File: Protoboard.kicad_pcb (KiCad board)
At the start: 2 copper layers, 103 x 140 mm, 92 parts, among them P1 CONN_01X08, P2 CONN_01X04, P3 CONN_01X05, P5 CONN_02X05, U1 LoLin_V3

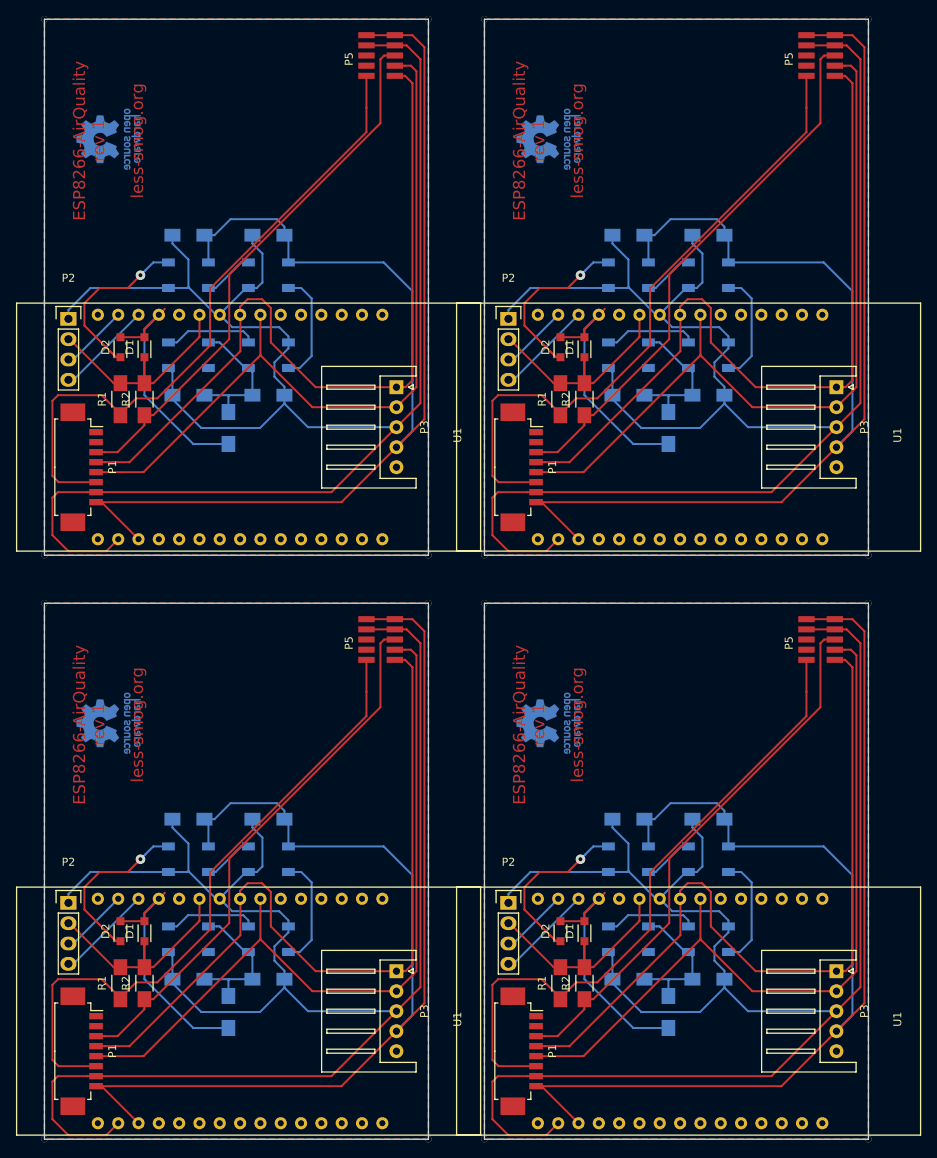
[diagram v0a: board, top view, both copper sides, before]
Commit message: Tigten boards together to fix on a 10x16 cm board.
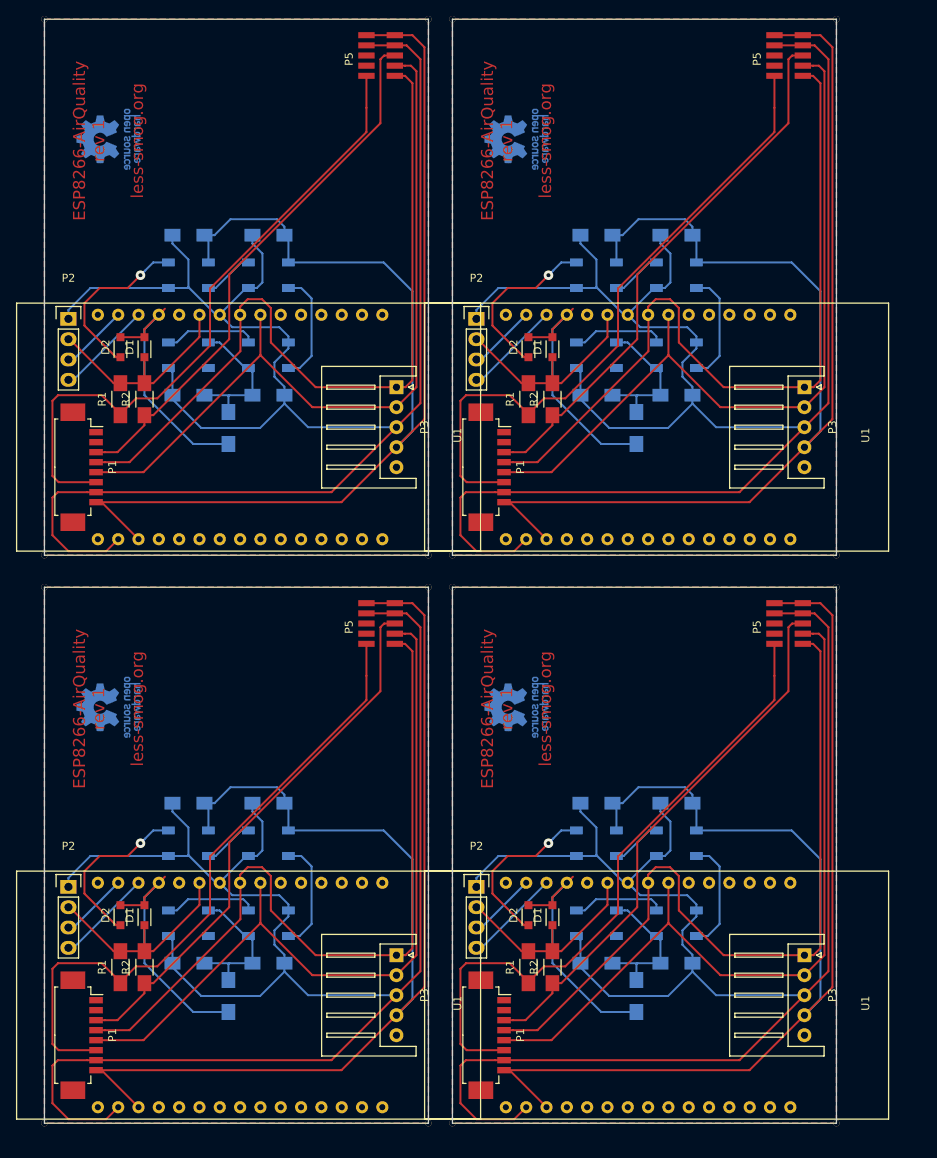
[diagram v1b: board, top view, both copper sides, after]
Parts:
- removed the ? at (74.1, 19.9)
- removed the ? at (74.1, 86.9)
- removed the ? at (74.1, 159.9)
- removed the ? at (19.1, 159.9)
- removed the ? at (67.1, 159.9)
- removed the ? at (67.1, 92.9)
- removed the ? at (19.1, 92.9)
- removed the ? at (74.1, 92.9)
- removed the ? at (122.1, 19.9)
- removed the ? at (122.1, 92.9)
- removed the ? at (122.1, 86.9)
- removed the ? at (122.1, 159.9)
- removed the C1 at (92.1, 46.9)
- removed the C1 at (92.1, 119.9)
- removed the C1 at (37.1, 119.9)
- removed the C2 at (102.1, 46.9)
- removed the C2 at (102.1, 119.9)
- removed the C2 at (47.1, 119.9)
- removed the C3 at (102.1, 66.9)
- removed the C3 at (102.1, 139.9)
- removed the C3 at (47.1, 139.9)
- removed the C4 at (92.1, 66.9)
- removed the C4 at (92.1, 139.9)
- removed the C4 at (37.1, 139.9)
- removed the D1 at (86.6, 60.9)
- removed the D1 at (86.6, 133.9)
- removed the D1 at (31.6, 133.9)
- removed the D2 at (83.6, 60.9)
- removed the D2 at (83.6, 133.9)
- removed the D2 at (28.6, 133.9)
- removed the LED1 at (92.1, 51.9)
- removed the LED1 at (92.1, 124.9)
- removed the LED1 at (37.1, 124.9)
- removed the LED2 at (102.1, 51.9)
- removed the LED2 at (102.1, 124.9)
- removed the LED2 at (47.1, 124.9)
- removed the LED3 at (102.1, 61.9)
- removed the LED3 at (102.1, 134.9)
- removed the LED3 at (47.1, 134.9)
- removed the LED4 at (92.1, 61.9)
- removed the LED4 at (92.1, 134.9)
- removed the LED4 at (37.1, 134.9)
- removed the P1 at (79.1, 75.9)
- removed the P1 at (79.1, 148.9)
- removed the P1 at (24.1, 148.9)
- removed the P2 at (77.1, 57.4)
- removed the P2 at (77.1, 130.4)
- removed the P2 at (22.1, 130.4)
- removed the P3 at (118.1, 65.9)
- removed the P3 at (118.1, 138.9)
- removed the P3 at (63.1, 138.9)
- removed the P5 at (114.3, 21.9)
- removed the P5 at (114.3, 94.9)
- removed the P5 at (59.3, 94.9)
- removed the R1 at (83.6, 67.4)
- removed the R1 at (83.6, 140.4)
- removed the R1 at (28.6, 140.4)
- removed the R2 at (86.6, 67.4)
- removed the R2 at (86.6, 140.4)
- removed the R2 at (31.6, 140.4)
- removed the R3 at (97.1, 71.0)
- removed the R3 at (97.1, 144.0)
- removed the R3 at (42.1, 144.0)
- removed the REF*** at (82.1, 34.9)
- removed the REF*** at (82.1, 107.9)
- removed the REF*** at (27.1, 107.9)
- removed the U1 at (70.6, 86.7)
- removed the U1 at (70.6, 159.7)
- removed the U1 at (15.6, 159.7)
- added ?: , Wire_Pads:SolderWirePad_single_0-8mmDrill, F.Cu at (118.1, 90.9)
- added ?: , Wire_Pads:SolderWirePad_single_0-8mmDrill, F.Cu at (70.1, 157.9)
- added ?: , Wire_Pads:SolderWirePad_single_0-8mmDrill, F.Cu at (19.1, 157.9)
- added ?: , Wire_Pads:SolderWirePad_single_0-8mmDrill, F.Cu at (70.1, 86.9)
- added ?: , Wire_Pads:SolderWirePad_single_0-8mmDrill, F.Cu at (67.1, 90.9)
- added ?: , Wire_Pads:SolderWirePad_single_0-8mmDrill, F.Cu at (118.1, 19.9)
- added ?: , Wire_Pads:SolderWirePad_single_0-8mmDrill, F.Cu at (70.1, 90.9)
- added ?: , Wire_Pads:SolderWirePad_single_0-8mmDrill, F.Cu at (19.1, 90.9)
- added ?: , Wire_Pads:SolderWirePad_single_0-8mmDrill, F.Cu at (70.1, 19.9)
- added ?: , Wire_Pads:SolderWirePad_single_0-8mmDrill, F.Cu at (118.1, 157.9)
- added ?: , Wire_Pads:SolderWirePad_single_0-8mmDrill, F.Cu at (67.1, 157.9)
- added ?: , Wire_Pads:SolderWirePad_single_0-8mmDrill, F.Cu at (118.1, 86.9)
- added C1: 100nF, Capacitors_SMD:C_1206_HandSoldering, B.Cu at (88.1, 117.9)
- added C1: 100nF, Capacitors_SMD:C_1206_HandSoldering, B.Cu at (37.1, 117.9)
- added C1: 100nF, Capacitors_SMD:C_1206_HandSoldering, B.Cu at (88.1, 46.9)
- added C2: 100nF, Capacitors_SMD:C_1206_HandSoldering, B.Cu at (98.1, 117.9)
- added C2: 100nF, Capacitors_SMD:C_1206_HandSoldering, B.Cu at (47.1, 117.9)
- added C2: 100nF, Capacitors_SMD:C_1206_HandSoldering, B.Cu at (98.1, 46.9)
- added C3: 100nF, Capacitors_SMD:C_1206_HandSoldering, B.Cu at (98.1, 137.9)
- added C3: 100nF, Capacitors_SMD:C_1206_HandSoldering, B.Cu at (47.1, 137.9)
- added C3: 100nF, Capacitors_SMD:C_1206_HandSoldering, B.Cu at (98.1, 66.9)
- added C4: 100nF, Capacitors_SMD:C_1206_HandSoldering, B.Cu at (88.1, 137.9)
- added C4: 100nF, Capacitors_SMD:C_1206_HandSoldering, B.Cu at (37.1, 137.9)
- added C4: 100nF, Capacitors_SMD:C_1206_HandSoldering, B.Cu at (88.1, 66.9)
- added D1: D, Diodes_SMD:SOD-323_HandSoldering, F.Cu at (82.6, 131.9)
- added D1: D, Diodes_SMD:SOD-323_HandSoldering, F.Cu at (31.6, 131.9)
- added D1: D, Diodes_SMD:SOD-323_HandSoldering, F.Cu at (82.6, 60.9)
- added D2: D, Diodes_SMD:SOD-323_HandSoldering, F.Cu at (79.6, 131.9)
- added D2: D, Diodes_SMD:SOD-323_HandSoldering, F.Cu at (28.6, 131.9)
- added D2: D, Diodes_SMD:SOD-323_HandSoldering, F.Cu at (79.6, 60.9)
- added LED1: WS2812B, LEDs:LED_WS2812B-PLCC4, B.Cu at (88.1, 122.9)
- added LED1: WS2812B, LEDs:LED_WS2812B-PLCC4, B.Cu at (37.1, 122.9)
- added LED1: WS2812B, LEDs:LED_WS2812B-PLCC4, B.Cu at (88.1, 51.9)
- added LED2: WS2812B, LEDs:LED_WS2812B-PLCC4, B.Cu at (98.1, 122.9)
- added LED2: WS2812B, LEDs:LED_WS2812B-PLCC4, B.Cu at (47.1, 122.9)
- added LED2: WS2812B, LEDs:LED_WS2812B-PLCC4, B.Cu at (98.1, 51.9)
- added LED3: WS2812B, LEDs:LED_WS2812B-PLCC4, B.Cu at (98.1, 132.9)
- added LED3: WS2812B, LEDs:LED_WS2812B-PLCC4, B.Cu at (47.1, 132.9)
- added LED3: WS2812B, LEDs:LED_WS2812B-PLCC4, B.Cu at (98.1, 61.9)
- added LED4: WS2812B, LEDs:LED_WS2812B-PLCC4, B.Cu at (88.1, 132.9)
- added LED4: WS2812B, LEDs:LED_WS2812B-PLCC4, B.Cu at (37.1, 132.9)
- added LED4: WS2812B, LEDs:LED_WS2812B-PLCC4, B.Cu at (88.1, 61.9)
- added P1: CONN_01X08, Connectors_Molex:Molex_PicoBlade_53261-0871_08x1.25mm_Angled, F.Cu at (75.1, 146.9)
- added P1: CONN_01X08, Connectors_Molex:Molex_PicoBlade_53261-0871_08x1.25mm_Angled, F.Cu at (24.1, 146.9)
- added P1: CONN_01X08, Connectors_Molex:Molex_PicoBlade_53261-0871_08x1.25mm_Angled, F.Cu at (75.1, 75.9)
- added P2: CONN_01X04, Pin_Headers:Pin_Header_Straight_1x04, F.Cu at (73.1, 128.4)
- added P2: CONN_01X04, Pin_Headers:Pin_Header_Straight_1x04, F.Cu at (22.1, 128.4)
- added P2: CONN_01X04, Pin_Headers:Pin_Header_Straight_1x04, F.Cu at (73.1, 57.4)
- added P3: CONN_01X05, Connectors_JST:JST_XH_S05B-XH-A_05x2.50mm_Angled, F.Cu at (114.1, 136.9)
- added P3: CONN_01X05, Connectors_JST:JST_XH_S05B-XH-A_05x2.50mm_Angled, F.Cu at (63.1, 136.9)
- added P3: CONN_01X05, Connectors_JST:JST_XH_S05B-XH-A_05x2.50mm_Angled, F.Cu at (114.1, 65.9)
- added P5: CONN_02X05, Amphenol:Amphenol, F.Cu at (110.3, 92.9)
- added P5: CONN_02X05, Amphenol:Amphenol, F.Cu at (59.3, 92.9)
- added P5: CONN_02X05, Amphenol:Amphenol, F.Cu at (110.3, 21.9)
- added R1: 10k, Resistors_SMD:R_1206_HandSoldering, F.Cu at (79.6, 138.4)
- added R1: 10k, Resistors_SMD:R_1206_HandSoldering, F.Cu at (28.6, 138.4)
- added R1: 10k, Resistors_SMD:R_1206_HandSoldering, F.Cu at (79.6, 67.4)
- added R2: 10k, Resistors_SMD:R_1206_HandSoldering, F.Cu at (82.6, 138.4)
- added R2: 10k, Resistors_SMD:R_1206_HandSoldering, F.Cu at (31.6, 138.4)
- added R2: 10k, Resistors_SMD:R_1206_HandSoldering, F.Cu at (82.6, 67.4)
- added R3: 10k, Resistors_SMD:R_1206_HandSoldering, B.Cu at (93.1, 142.0)
- added R3: 10k, Resistors_SMD:R_1206_HandSoldering, B.Cu at (42.1, 142.0)
- added R3: 10k, Resistors_SMD:R_1206_HandSoldering, B.Cu at (93.1, 71.0)
- added REF***: OSHW-Logo_7.5x8mm_Copper, Symbols:OSHW-Logo_7.5x8mm_Copper, B.Cu at (78.1, 105.9)
- added REF***: OSHW-Logo_7.5x8mm_Copper, Symbols:OSHW-Logo_7.5x8mm_Copper, B.Cu at (27.1, 105.9)
- added REF***: OSHW-Logo_7.5x8mm_Copper, Symbols:OSHW-Logo_7.5x8mm_Copper, B.Cu at (78.1, 34.9)
- added U1: LoLin_V3, LoLin:LoLin, F.Cu at (66.6, 157.7)
- added U1: LoLin_V3, LoLin:LoLin, F.Cu at (15.6, 157.7)
- added U1: LoLin_V3, LoLin:LoLin, F.Cu at (66.6, 86.7)
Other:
- board size 103 x 140 mm -> 99 x 138 mm

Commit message: Removed drilling holes from corners and regenerated drill file.
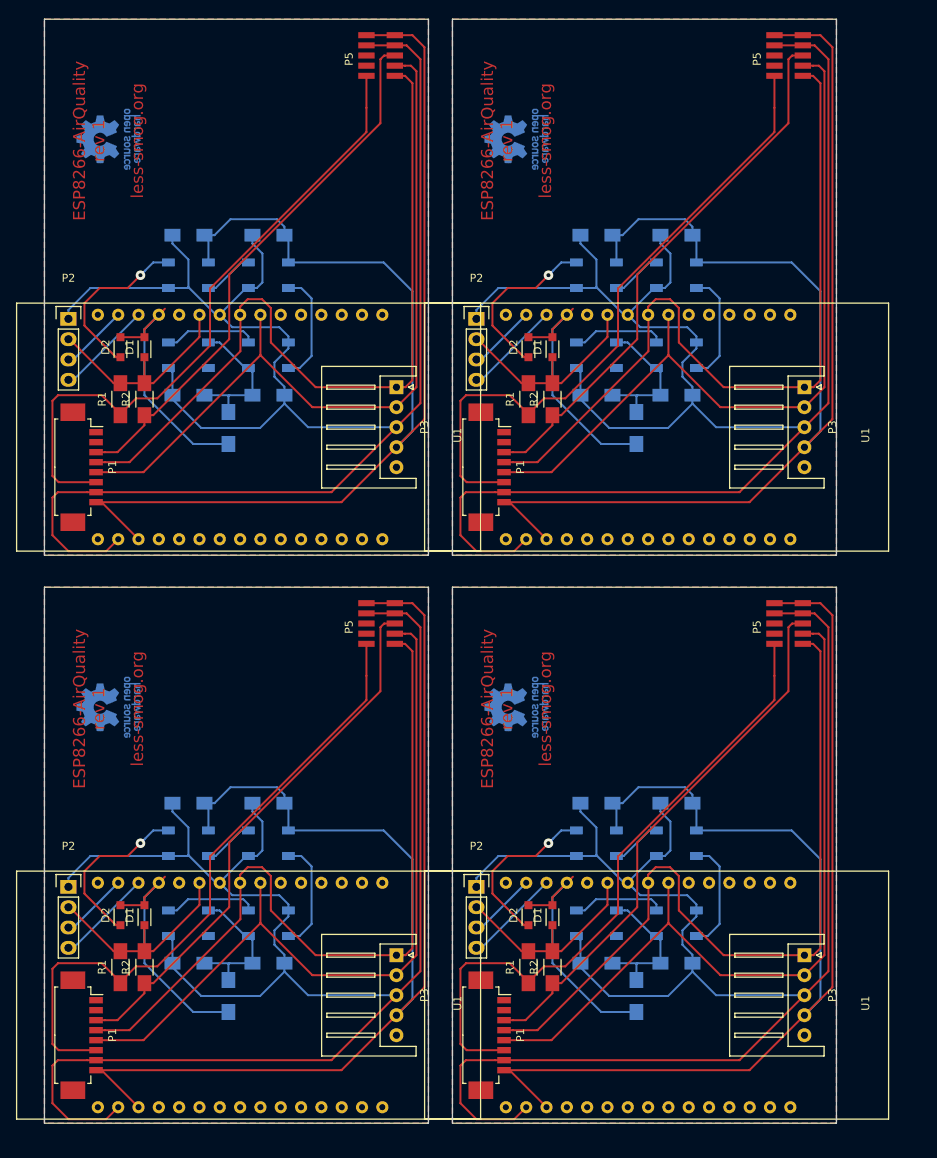
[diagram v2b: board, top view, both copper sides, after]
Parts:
- removed ? (x16): , Wire_Pads:SolderWirePad_single_0-8mmDrill
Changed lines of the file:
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@@
     (links 262)
     (no_connects 54)
-    (area 15.1375 19.33245 128.862501 160.53255)
+    (area 15.1375 19.33245 124.862501 158.53255)
     (thickness 1.6)
     (drawings 20)
     (tracks 720)
     (zones 0)
-    (modules 92)
+    (modules 76)
     (nets 15)
   )
@@
     )
   )
-  (module Wire_Pads:SolderWirePad_single_0-8mmDrill (layer F.Cu)
-    (at 118.0675 90.9325 90)
-    (fp_text reference "" (at 0 -2.54 90) (layer F.SilkS)
-      (effects (font (size 1 1) (thickness 0.15)))
-    )
-    (fp_text value "" (at 0 2.54 90) (layer F.Fab)
-      (effects (font (size 1 1) (thickness 0.15)))
-    )
-    (pad 1 thru_hole circle (at 0 0 90) (size 0.8001 0.8001) (drill 0.8001) (layers *.Cu *.Mask))
-  )
-  (module Wire_Pads:SolderWirePad_single_0-8mmDrill (layer F.Cu)
-    (at 67.0675 90.9325 90)
-    (fp_text reference "" (at 0 -2.54 90) (layer F.SilkS)
-      (effects (font (size 1 1) (thickness 0.15)))
-    )
-    (fp_text value "" (at 0 2.54 90) (layer F.Fab)
-      (effects (font (size 1 1) (thickness 0.15)))
-    )
-    (pad 1 thru_hole circle (at 0 0 90) (size 0.8001 0.8001) (drill 0.8001) (layers *.Cu *.Mask))
-  )
-  (module Wire_Pads:SolderWirePad_single_0-8mmDrill (layer F.Cu)
-    (at 118.0675 19.9325 90)
-    (fp_text reference "" (at 0 -2.54 90) (layer F.SilkS)
-      (effects (font (size 1 1) (thickness 0.15)))
-    )
-    (fp_text value "" (at 0 2.54 90) (layer F.Fab)
-      (effects (font (size 1 1) (thickness 0.15)))
-    )
-    (pad 1 thru_hole circle (at 0 0 90) (size 0.8001 0.8001) (drill 0.8001) (layers *.Cu *.Mask))
-  )
   (module Amphenol:Amphenol (layer F.Cu)
     (at 110.3175 92.9325 270)
@@
     )
   )
-  (module Wire_Pads:SolderWirePad_single_0-8mmDrill (layer F.Cu)
-    (at 70.0675 90.9325 90)
-    (fp_text reference "" (at 0 -2.54 90) (layer F.SilkS)
-      (effects (font (size 1 1) (thickness 0.15)))
-    )
-    (fp_text value "" (at 0 2.54 90) (layer F.Fab)
-      (effects (font (size 1 1) (thickness 0.15)))
-    )
-    (pad 1 thru_hole circle (at 0 0 90) (size 0.8001 0.8001) (drill 0.8001) (layers *.Cu *.Mask))
-  )
-  (module Wire_Pads:SolderWirePad_single_0-8mmDrill (layer F.Cu)
-    (at 19.0675 90.9325 90)
-    (fp_text reference "" (at 0 -2.54 90) (layer F.SilkS)
-      (effects (font (size 1 1) (thickness 0.15)))
-    )
-    (fp_text value "" (at 0 2.54 90) (layer F.Fab)
-      (effects (font (size 1 1) (thickness 0.15)))
-    )
-    (pad 1 thru_hole circle (at 0 0 90) (size 0.8001 0.8001) (drill 0.8001) (layers *.Cu *.Mask))
-  )
-  (module Wire_Pads:SolderWirePad_single_0-8mmDrill (layer F.Cu)
-    (at 70.0675 19.9325 90)
-    (fp_text reference "" (at 0 -2.54 90) (layer F.SilkS)
-      (effects (font (size 1 1) (thickness 0.15)))
-    )
-    (fp_text value "" (at 0 2.54 90) (layer F.Fab)
-      (effects (font (size 1 1) (thickness 0.15)))
-    )
-    (pad 1 thru_hole circle (at 0 0 90) (size 0.8001 0.8001) (drill 0.8001) (layers *.Cu *.Mask))
-  )
-  (module Wire_Pads:SolderWirePad_single_0-8mmDrill (layer F.Cu)
-    (at 118.0675 157.9325 90)
-    (fp_text reference "" (at 0 -2.54 90) (layer F.SilkS)
-      (effects (font (size 1 1) (thickness 0.15)))
-    )
-    (fp_text value "" (at 0 2.54 90) (layer F.Fab)
-      (effects (font (size 1 1) (thickness 0.15)))
-    )
-    (pad 1 thru_hole circle (at 0 0 90) (size 0.8001 0.8001) (drill 0.8001) (layers *.Cu *.Mask))
-  )
-  (module Wire_Pads:SolderWirePad_single_0-8mmDrill (layer F.Cu)
-    (at 67.0675 157.9325 90)
-    (fp_text reference "" (at 0 -2.54 90) (layer F.SilkS)
-      (effects (font (size 1 1) (thickness 0.15)))
-    )
-    (fp_text value "" (at 0 2.54 90) (layer F.Fab)
-      (effects (font (size 1 1) (thickness 0.15)))
-    )
-    (pad 1 thru_hole circle (at 0 0 90) (size 0.8001 0.8001) (drill 0.8001) (layers *.Cu *.Mask))
-  )
-  (module Wire_Pads:SolderWirePad_single_0-8mmDrill (layer F.Cu)
-    (at 118.0675 86.9325 90)
-    (fp_text reference "" (at 0 -2.54 90) (layer F.SilkS)
-      (effects (font (size 1 1) (thickness 0.15)))
-    )
-    (fp_text value "" (at 0 2.54 90) (layer F.Fab)
-      (effects (font (size 1 1) (thickness 0.15)))
-    )
-    (pad 1 thru_hole circle (at 0 0 90) (size 0.8001 0.8001) (drill 0.8001) (layers *.Cu *.Mask))
-  )
   (module Connectors_JST:JST_XH_S05B-XH-A_05x2.50mm_Angled (layer F.Cu)
     (at 114.0675 136.9325 270)
@@
     )
   )
-  (module Wire_Pads:SolderWirePad_single_0-8mmDrill (layer F.Cu)
-    (at 70.0675 157.9325 90)
-    (fp_text reference "" (at 0 -2.54 90) (layer F.SilkS)
-      (effects (font (size 1 1) (thickness 0.15)))
-    )
-    (fp_text value "" (at 0 2.54 90) (layer F.Fab)
-      (effects (font (size 1 1) (thickness 0.15)))
-    )
-    (pad 1 thru_hole circle (at 0 0 90) (size 0.8001 0.8001) (drill 0.8001) (layers *.Cu *.Mask))
-  )
-  (module Wire_Pads:SolderWirePad_single_0-8mmDrill (layer F.Cu)
-    (at 19.0675 157.9325 90)
-    (fp_text reference "" (at 0 -2.54 90) (layer F.SilkS)
-      (effects (font (size 1 1) (thickness 0.15)))
-    )
-    (fp_text value "" (at 0 2.54 90) (layer F.Fab)
-      (effects (font (size 1 1) (thickness 0.15)))
-    )
-    (pad 1 thru_hole circle (at 0 0 90) (size 0.8001 0.8001) (drill 0.8001) (layers *.Cu *.Mask))
-  )
-  (module Wire_Pads:SolderWirePad_single_0-8mmDrill (layer F.Cu)
-    (at 70.0675 86.9325 90)
-    (fp_text reference "" (at 0 -2.54 90) (layer F.SilkS)
-      (effects (font (size 1 1) (thickness 0.15)))
-    )
-    (fp_text value "" (at 0 2.54 90) (layer F.Fab)
-      (effects (font (size 1 1) (thickness 0.15)))
-    )
-    (pad 1 thru_hole circle (at 0 0 90) (size 0.8001 0.8001) (drill 0.8001) (layers *.Cu *.Mask))
-  )
   (module Pin_Headers:Pin_Header_Straight_1x04 (layer F.Cu)
     (at 73.0675 128.3925)
@@
     )
   )
-  (module Wire_Pads:SolderWirePad_single_0-8mmDrill (layer F.Cu)
-    (at 19.0675 19.9325 90)
-    (fp_text reference "" (at 0 -2.54 90) (layer F.SilkS)
-      (effects (font (size 1 1) (thickness 0.15)))
-    )
-    (fp_text value "" (at 0 2.54 90) (layer F.Fab)
-      (effects (font (size 1 1) (thickness 0.15)))
-    )
-    (pad 1 thru_hole circle (at 0 0 90) (size 0.8001 0.8001) (drill 0.8001) (layers *.Cu *.Mask))
-  )
   (module Amphenol:Amphenol (layer F.Cu)
     (at 59.3175 21.9325 270)
@@
       (net 10 TXD))
   )
-  (module Wire_Pads:SolderWirePad_single_0-8mmDrill (layer F.Cu)
-    (at 67.0675 19.9325 90)
-    (fp_text reference "" (at 0 -2.54 90) (layer F.SilkS)
-      (effects (font (size 1 1) (thickness 0.15)))
-    )
-    (fp_text value "" (at 0 2.54 90) (layer F.Fab)
-      (effects (font (size 1 1) (thickness 0.15)))
-    )
-    (pad 1 thru_hole circle (at 0 0 90) (size 0.8001 0.8001) (drill 0.8001) (layers *.Cu *.Mask))
-  )
-  (module Wire_Pads:SolderWirePad_single_0-8mmDrill (layer F.Cu)
-    (at 67.0675 86.9325 90)
-    (fp_text reference "" (at 0 -2.54 90) (layer F.SilkS)
-      (effects (font (size 1 1) (thickness 0.15)))
-    )
-    (fp_text value "" (at 0 2.54 90) (layer F.Fab)
-      (effects (font (size 1 1) (thickness 0.15)))
-    )
-    (pad 1 thru_hole circle (at 0 0 90) (size 0.8001 0.8001) (drill 0.8001) (layers *.Cu *.Mask))
-  )
   (module Connectors_JST:JST_XH_S05B-XH-A_05x2.50mm_Angled (layer F.Cu)
     (at 63.0675 65.9325 270)
@@
     )
   )
-  (module Wire_Pads:SolderWirePad_single_0-8mmDrill (layer F.Cu)
-    (at 19.0675 86.9325 90)
-    (fp_text reference "" (at 0 -2.54 90) (layer F.SilkS)
-      (effects (font (size 1 1) (thickness 0.15)))
-    )
-    (fp_text value "" (at 0 2.54 90) (layer F.Fab)
-      (effects (font (size 1 1) (thickness 0.15)))
-    )
-    (pad 1 thru_hole circle (at 0 0 90) (size 0.8001 0.8001) (drill 0.8001) (layers *.Cu *.Mask))
-  )
   (gr_line (start 70.0675 157.9325) (end 70.0675 90.9325) (layer Edge.Cuts) (width 0.15))
